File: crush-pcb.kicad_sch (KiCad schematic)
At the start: 9 parts, among them J1 TSW-108-07-G-T, J2 USB_B_Micro, U1 Teensy4.1, U2 ISO7740DW, U3 ISO7740DW

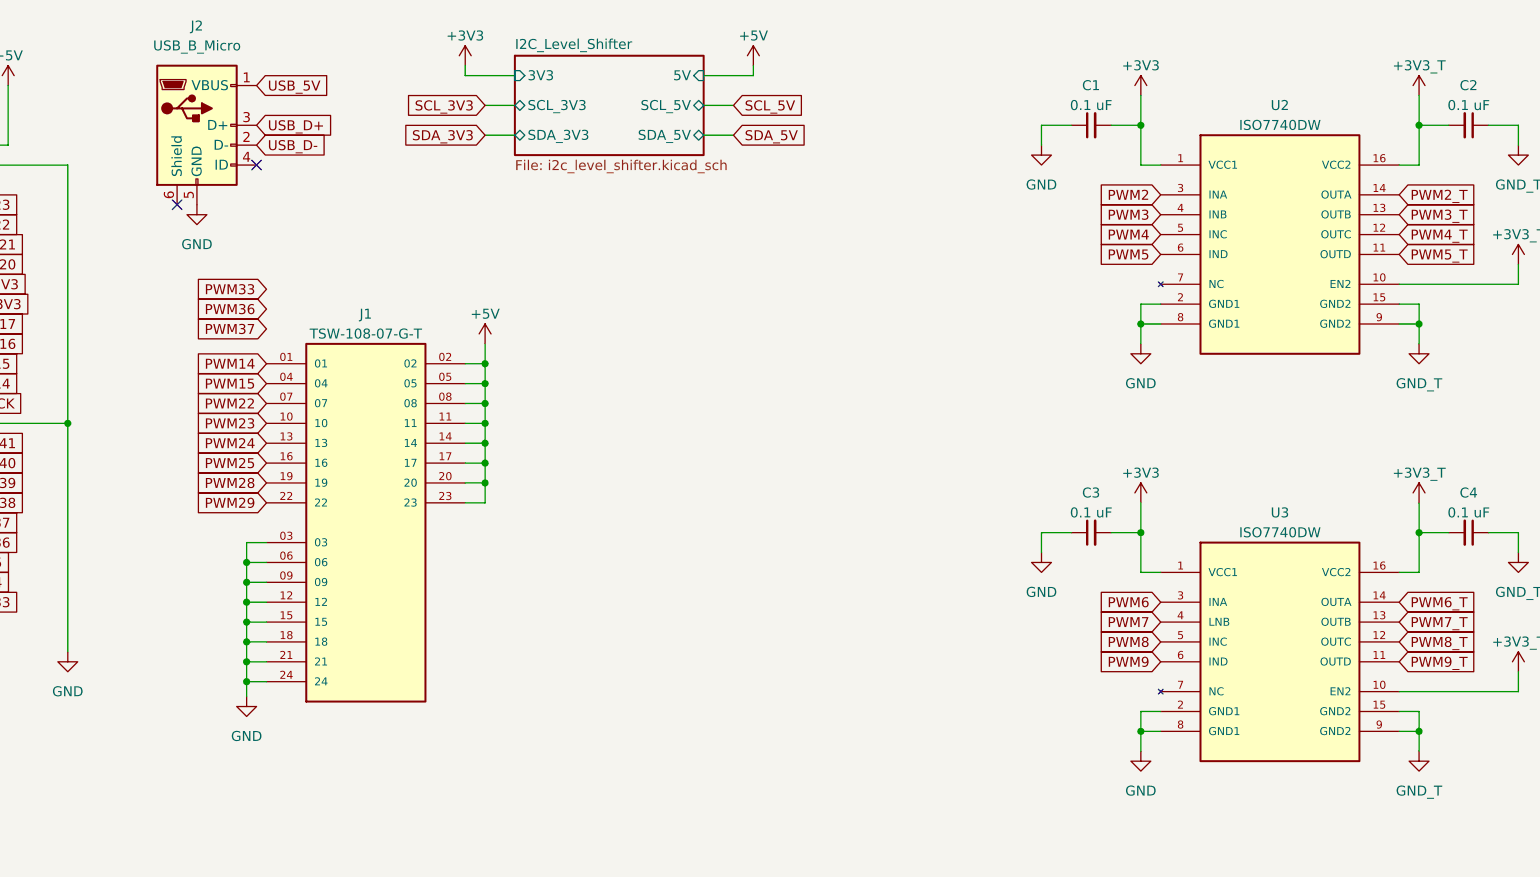
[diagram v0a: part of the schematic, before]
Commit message: Update custom library and add PWM headers
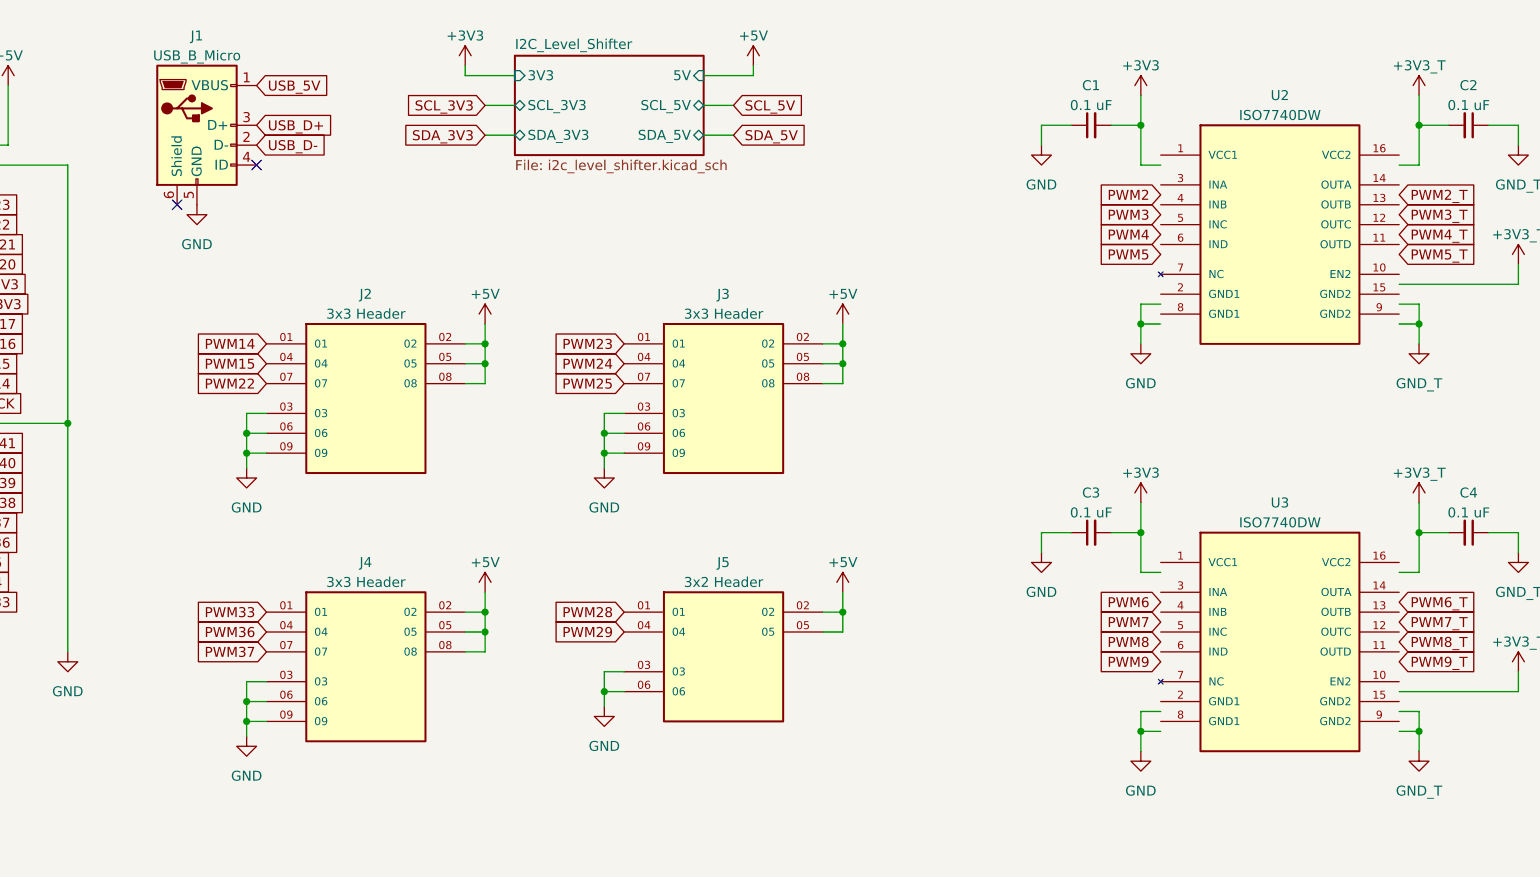
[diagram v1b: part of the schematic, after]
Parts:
- removed J1: TSW-108-07-G-T, SAMTEC_TSW-108-07-G-T, symbol 3x8 Header:TSW-108-07-G-T
- added J2, J3, J4: 3x3 Header, symbol CrushMainBoard_Library:3x3_Header
- added J5: 3x2 Header, symbol CrushMainBoard_Library:3x2_Header
- U2, U3: symbol ISO7740DW:ISO7740DW -> CrushMainBoard_Library:ISO7740DW
- renumbered J2 to J1
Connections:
- net +3V3: no longer U2.1 (VCC1), U2.10 (EN2), U2.16 (VCC2), U3.1 (VCC1), U3.10 (EN2), U3.16 (VCC2)
- net +5V: now also J2.02, J2.05, J2.08, J3.02, J3.05, J3.08, J4.02, J4.05, J4.08, J5.02, J5.05
- net GND: now also J2.03, J2.06, J2.09, J3.03, J3.06, J3.09, J4.03, J4.06, J4.09, J5.03, J5.06; no longer U2.15 (GND2), U2.2 (GND1), U2.8 (GND1), U2.9 (GND2), U3.15 (GND2), U3.2 (GND1), U3.8 (GND1), U3.9 (GND2)
- net PWM14: now also J2.01
- net PWM15: now also J2.04
- net PWM2: no longer U2.3 (INA)
- net PWM22: now also J2.07
- net PWM23: now also J3.01
- net PWM24: now also J3.04
- net PWM25: now also J3.07
- net PWM28: now also J5.01
- net PWM29: now also J5.04
- net PWM2_T: no longer U2.14 (OUTA)
- net PWM3: no longer U2.4 (INB)
- net PWM33: now also J4.01
- net PWM36: now also J4.04
- net PWM37: now also J4.07
- net PWM3_T: no longer U2.13 (OUTB)
- net PWM4: no longer U2.5 (INC)
- net PWM4_T: no longer U2.12 (OUTC)
- net PWM5: no longer U2.6 (IND)
- net PWM5_T: no longer U2.11 (OUTD)
- net PWM6: no longer U3.3 (INA)
- net PWM6_T: no longer U3.14 (OUTA)
- net PWM7: no longer U3.4 (LNB)
- net PWM7_T: no longer U3.13 (OUTB)
- net PWM8: no longer U3.5 (INC)
- net PWM8_T: no longer U3.12 (OUTC)
- net PWM9: no longer U3.6 (IND)
- net PWM9_T: no longer U3.11 (OUTD)
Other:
- moved on the sheet: U2, U3

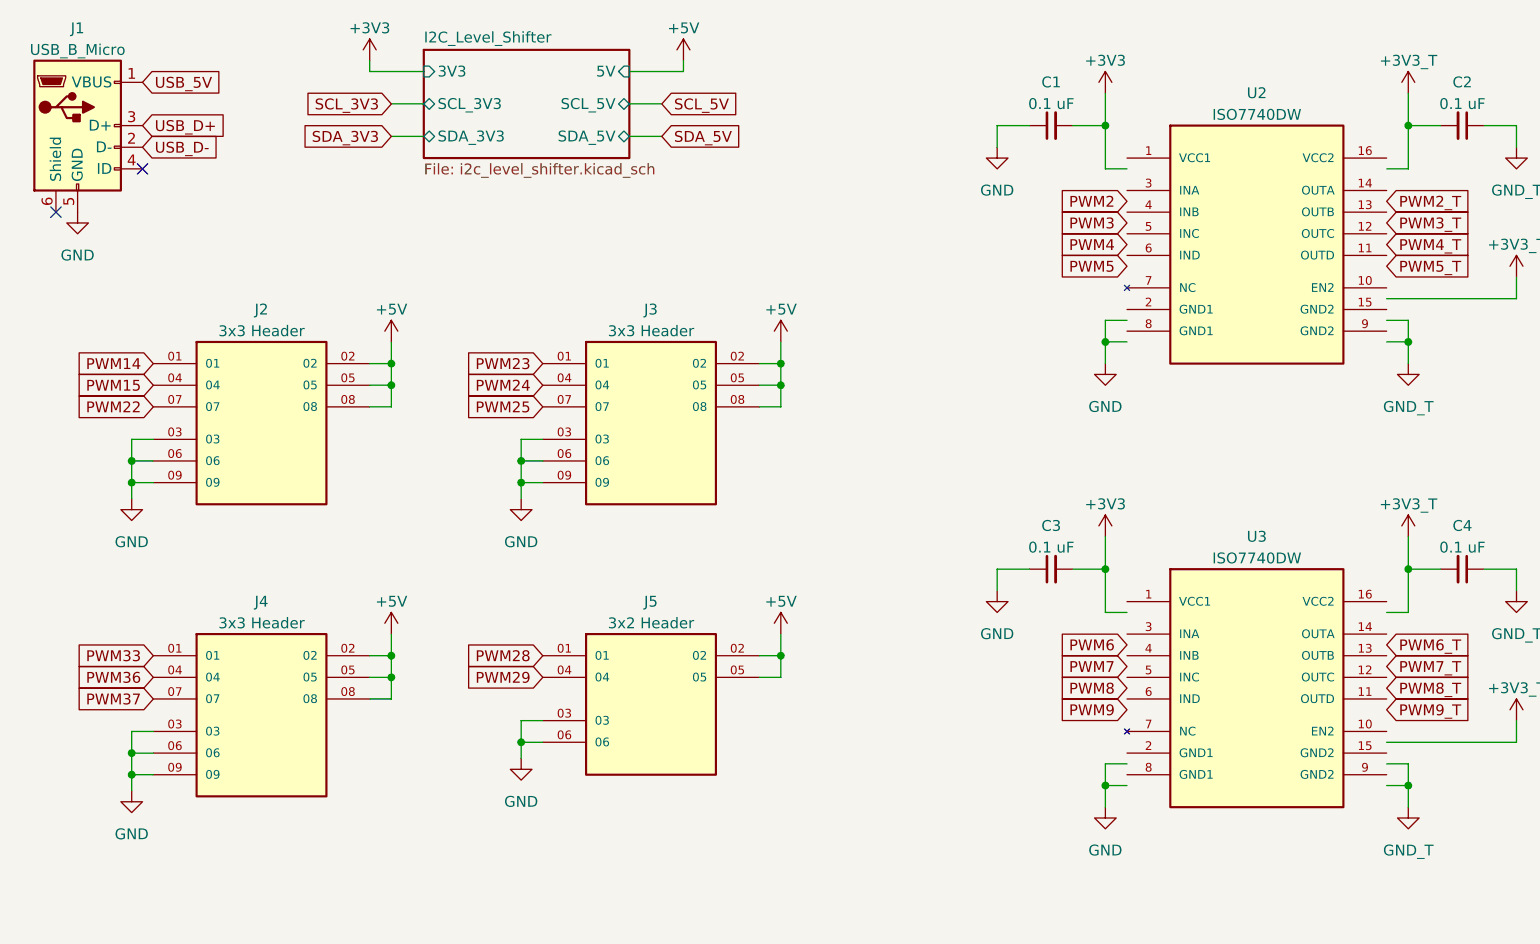
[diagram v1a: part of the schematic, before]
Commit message: Library Update
Add the footprint library named "Crush_Mainboard_Footprints.pretty" in the library folder
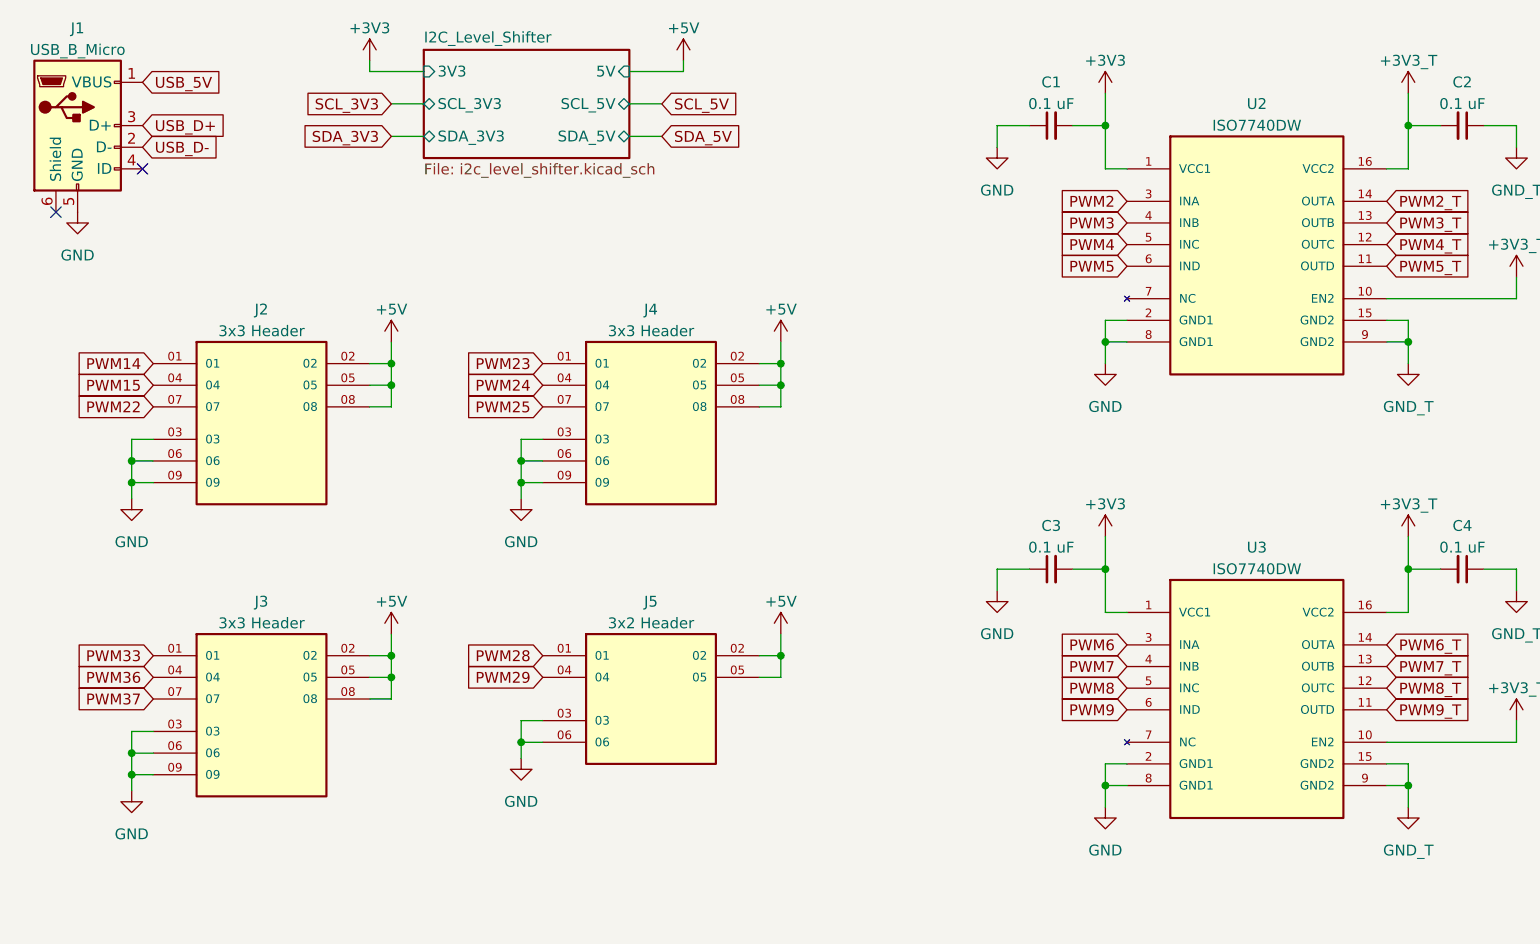
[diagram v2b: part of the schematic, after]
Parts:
- U2, U3: footprint SOIC127P1030X265-16N -> Crush_Mainboard_Footprints:SOIC127P1030X265-16N
- renumbered J4 to J3, J3 to J4
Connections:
- net +3V3: now also U2.1 (VCC1), U2.10 (EN2), U2.16 (VCC2), U3.1 (VCC1), U3.10 (EN2), U3.16 (VCC2)
- net GND: now also U2.15 (GND2), U2.2 (GND1), U2.8 (GND1), U2.9 (GND2), U3.15 (GND2), U3.2 (GND1), U3.8 (GND1), U3.9 (GND2)
- net PWM2: now also U2.3 (INA)
- net PWM2_T: now also U2.14 (OUTA)
- net PWM3: now also U2.4 (INB)
- net PWM3_T: now also U2.13 (OUTB)
- net PWM4: now also U2.5 (INC)
- net PWM4_T: now also U2.12 (OUTC)
- net PWM5: now also U2.6 (IND)
- net PWM5_T: now also U2.11 (OUTD)
- net PWM6: now also U3.3 (INA)
- net PWM6_T: now also U3.14 (OUTA)
- net PWM7: now also U3.4 (INB)
- net PWM7_T: now also U3.13 (OUTB)
- net PWM8: now also U3.5 (INC)
- net PWM8_T: now also U3.12 (OUTC)
- net PWM9: now also U3.6 (IND)
- net PWM9_T: now also U3.11 (OUTD)
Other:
- moved on the sheet: J5, U2, U3
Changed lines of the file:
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@@
     )
   )
-  (symbol (lib_id "CrushMainBoard_Library:ISO7740DW") (at 251.46 82.55 0) (unit 1)
-    (in_bom yes) (on_board yes) (dnp no) (fields_autoplaced)
-    (property "Reference" "U3" (at 251.46 64.77 0)
-      (effects (font (size 1.27 1.27)))
-    )
-    (property "Value" "ISO7740DW" (at 251.46 67.31 0)
-      (effects (font (size 1.27 1.27)))
-    )
-    (property "Footprint" "SOIC127P1030X265-16N" (at 251.46 82.55 0)
-      (effects (font (size 1.27 1.27)) (justify bottom) hide)
-    )
-    (property "Datasheet" "" (at 251.46 81.28 0)
+  (symbol (lib_id "CrushMainBoard_Library:ISO7740DW") (at 251.46 83.82 0) (unit 1)
+    (in_bom yes) (on_board yes) (dnp no) (fields_autoplaced)
+    (property "Reference" "U3" (at 251.46 66.04 0)
+      (effects (font (size 1.27 1.27)))
+    )
+    (property "Value" "ISO7740DW" (at 251.46 68.58 0)
+      (effects (font (size 1.27 1.27)))
+    )
+    (property "Footprint" "Crush_Mainboard_Footprints:SOIC127P1030X265-16N" (at 251.46 83.82 0)
+      (effects (font (size 1.27 1.27)) (justify bottom) hide)
+    )
+    (property "Datasheet" "" (at 251.46 82.55 0)
       (effects (font (size 1.27 1.27)) hide)
     )
@@
     )
   )
-  (symbol (lib_id "CrushMainBoard_Library:3x3_Header") (at 134.62 83.82 0) (unit 1)
-    (in_bom yes) (on_board yes) (dnp no) (fields_autoplaced)
-    (property "Reference" "J4" (at 134.62 72.39 0)
+  (symbol (lib_id "CrushMainBoard_Library:3x3_Header") (at 134.62 85.725 0) (unit 1)
+    (in_bom yes) (on_board yes) (dnp no)
+    (property "Reference" "J3" (at 134.62 72.39 0)
       (effects (font (size 1.27 1.27)))
     )
@@
       (effects (font (size 1.27 1.27)))
     )
-    (property "Footprint" "" (at 157.48 95.25 0)
-      (effects (font (size 1.27 1.27)) (justify bottom) hide)
-    )
-    (property "Datasheet" "" (at 134.62 99.06 0)
-      (effects (font (size 1.27 1.27)) hide)
-    )
-    (property "PARTREV" "" (at 154.94 97.79 0)
-      (effects (font (size 1.27 1.27)) (justify bottom) hide)
-    )
-    (property "STANDARD" "" (at 161.29 113.03 0)
-      (effects (font (size 1.27 1.27)) (justify bottom) hide)
-    )
-    (property "MANUFACTURER" "" (at 134.62 99.06 0)
+    (property "Footprint" "" (at 157.48 97.155 0)
+      (effects (font (size 1.27 1.27)) (justify bottom) hide)
+    )
+    (property "Datasheet" "" (at 134.62 100.965 0)
+      (effects (font (size 1.27 1.27)) hide)
+    )
+    (property "PARTREV" "" (at 154.94 99.695 0)
+      (effects (font (size 1.27 1.27)) (justify bottom) hide)
+    )
+    (property "STANDARD" "" (at 161.29 114.935 0)
+      (effects (font (size 1.27 1.27)) (justify bottom) hide)
+    )
+    (property "MANUFACTURER" "" (at 134.62 100.965 0)
       (effects (font (size 1.27 1.27)) (justify bottom) hide)
     )
@@
       (project "crush-pcb"
         (path "/74b566fe-9d71-4817-95ed-d472d647f8c8"
-          (reference "J4") (unit 1)
+          (reference "J3") (unit 1)
         )
       )
@@
     )
   )
-  (symbol (lib_id "CrushMainBoard_Library:3x3_Header") (at 134.62 49.53 0) (unit 1)
-    (in_bom yes) (on_board yes) (dnp no) (fields_autoplaced)
+  (symbol (lib_id "CrushMainBoard_Library:3x3_Header") (at 134.62 51.435 0) (unit 1)
+    (in_bom yes) (on_board yes) (dnp no)
     (property "Reference" "J2" (at 134.62 38.1 0)
       (effects (font (size 1.27 1.27)))
@@
       (effects (font (size 1.27 1.27)))
     )
-    (property "Footprint" "" (at 157.48 60.96 0)
-      (effects (font (size 1.27 1.27)) (justify bottom) hide)
-    )
-    (property "Datasheet" "" (at 134.62 64.77 0)
-      (effects (font (size 1.27 1.27)) hide)
-    )
-    (property "PARTREV" "" (at 154.94 63.5 0)
-      (effects (font (size 1.27 1.27)) (justify bottom) hide)
-    )
-    (property "STANDARD" "" (at 161.29 78.74 0)
-      (effects (font (size 1.27 1.27)) (justify bottom) hide)
-    )
-    (property "MANUFACTURER" "" (at 134.62 64.77 0)
+    (property "Footprint" "" (at 157.48 62.865 0)
+      (effects (font (size 1.27 1.27)) (justify bottom) hide)
+    )
+    (property "Datasheet" "" (at 134.62 66.675 0)
+      (effects (font (size 1.27 1.27)) hide)
+    )
+    (property "PARTREV" "" (at 154.94 65.405 0)
+      (effects (font (size 1.27 1.27)) (justify bottom) hide)
+    )
+    (property "STANDARD" "" (at 161.29 80.645 0)
+      (effects (font (size 1.27 1.27)) (justify bottom) hide)
+    )
+    (property "MANUFACTURER" "" (at 134.62 66.675 0)
       (effects (font (size 1.27 1.27)) (justify bottom) hide)
     )
@@
     )
   )
-  (symbol (lib_id "CrushMainBoard_Library:3x3_Header") (at 180.34 49.53 0) (unit 1)
-    (in_bom yes) (on_board yes) (dnp no) (fields_autoplaced)
-    (property "Reference" "J3" (at 180.34 38.1 0)
+  (symbol (lib_id "CrushMainBoard_Library:3x3_Header") (at 180.34 51.435 0) (unit 1)
+    (in_bom yes) (on_board yes) (dnp no)
+    (property "Reference" "J4" (at 180.34 38.1 0)
       (effects (font (size 1.27 1.27)))
     )
@@
       (effects (font (size 1.27 1.27)))
     )
-    (property "Footprint" "" (at 203.2 60.96 0)
-      (effects (font (size 1.27 1.27)) (justify bottom) hide)
-    )
-    (property "Datasheet" "" (at 180.34 64.77 0)
-      (effects (font (size 1.27 1.27)) hide)
-    )
-    (property "PARTREV" "" (at 200.66 63.5 0)
-      (effects (font (size 1.27 1.27)) (justify bottom) hide)
-    )
-    (property "STANDARD" "" (at 207.01 78.74 0)
-      (effects (font (size 1.27 1.27)) (justify bottom) hide)
-    )
-    (property "MANUFACTURER" "" (at 180.34 64.77 0)
+    (property "Footprint" "" (at 203.2 62.865 0)
+      (effects (font (size 1.27 1.27)) (justify bottom) hide)
+    )
+    (property "Datasheet" "" (at 180.34 66.675 0)
+      (effects (font (size 1.27 1.27)) hide)
+    )
+    (property "PARTREV" "" (at 200.66 65.405 0)
+      (effects (font (size 1.27 1.27)) (justify bottom) hide)
+    )
+    (property "STANDARD" "" (at 207.01 80.645 0)
+      (effects (font (size 1.27 1.27)) (justify bottom) hide)
+    )
+    (property "MANUFACTURER" "" (at 180.34 66.675 0)
       (effects (font (size 1.27 1.27)) (justify bottom) hide)
     )
@@
       (project "crush-pcb"
         (path "/74b566fe-9d71-4817-95ed-d472d647f8c8"
-          (reference "J3") (unit 1)
+          (reference "J4") (unit 1)
         )
       )
@@
     )
   )
-  (symbol (lib_id "CrushMainBoard_Library:ISO7740DW") (at 251.46 30.48 0) (unit 1)
-    (in_bom yes) (on_board yes) (dnp no) (fields_autoplaced)
-    (property "Reference" "U2" (at 251.46 12.7 0)
-      (effects (font (size 1.27 1.27)))
-    )
-    (property "Value" "ISO7740DW" (at 251.46 15.24 0)
-      (effects (font (size 1.27 1.27)))
-    )
-    (property "Footprint" "SOIC127P1030X265-16N" (at 251.46 30.48 0)
-      (effects (font (size 1.27 1.27)) (justify bottom) hide)
-    )
-    (property "Datasheet" "" (at 251.46 29.21 0)
-      (effects (font (size 1.27 1.27)) hide)
-    )
+  (symbol (lib_id "CrushMainBoard_Library:ISO7740DW") (at 251.46 31.75 0) (unit 1)
+    (in_bom yes) (on_board yes) (dnp no) (fields_autoplaced)
+    (property "Reference" "U2" (at 251.46 13.97 0)
+      (effects (font (size 1.27 1.27)))
+    )
+    (property "Value" "ISO7740DW" (at 251.46 16.51 0)
+      (effects (font (size 1.27 1.27)))
+    )
+    (property "Footprint" "Crush_Mainboard_Footprints:SOIC127P1030X265-16N" (at 251.46 31.75 0)
+      (effects (font (size 1.27 1.27)) (justify bottom) hide)
+    )
+    (property "Datasheet" "" (at 251.46 30.48 0)
+      (effects (font (size 1.27 1.27)) hide)
+    )
